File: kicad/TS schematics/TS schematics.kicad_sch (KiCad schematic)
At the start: 40 parts, among them J1 Conn_01x05, J10 Amphenol PL00Y-301-10M8, J11 Amphenol RT00104PN03, J12 Amphenol PL00X-301-10M8, J13 AT04-4P-PM11, J14 紅色儲能接綫柱100A, J15 黑色儲能接綫柱100A, J16 Amphenol PL00X-301-10M8, J17 Amphenol PL00Y-301-10M8, J19 Amphenol RT001619SNHEC03, J2 TSAL_R, J23 AT04-3P-PM05, J24 Conn_01x02, J29 Amphenol RT001619PNH, J30 Conn_01x02, J31 Conn_01x06, J33 LEM DHAB S/124, J4 TSMP, J5 Amphenol RT00122PM03, J6 Amphenol RT00122PM03, J7 Amphenol RT001619PNH, J8 DALY K40 BMS, J9 Amphenol RT0W0106PN03, K1 DISCHARGE RELAY GIGAVAC PNC11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, SW19 BOTS, U1 dumb ass dcdc 15V8A 120W, U2 CCCV 300W

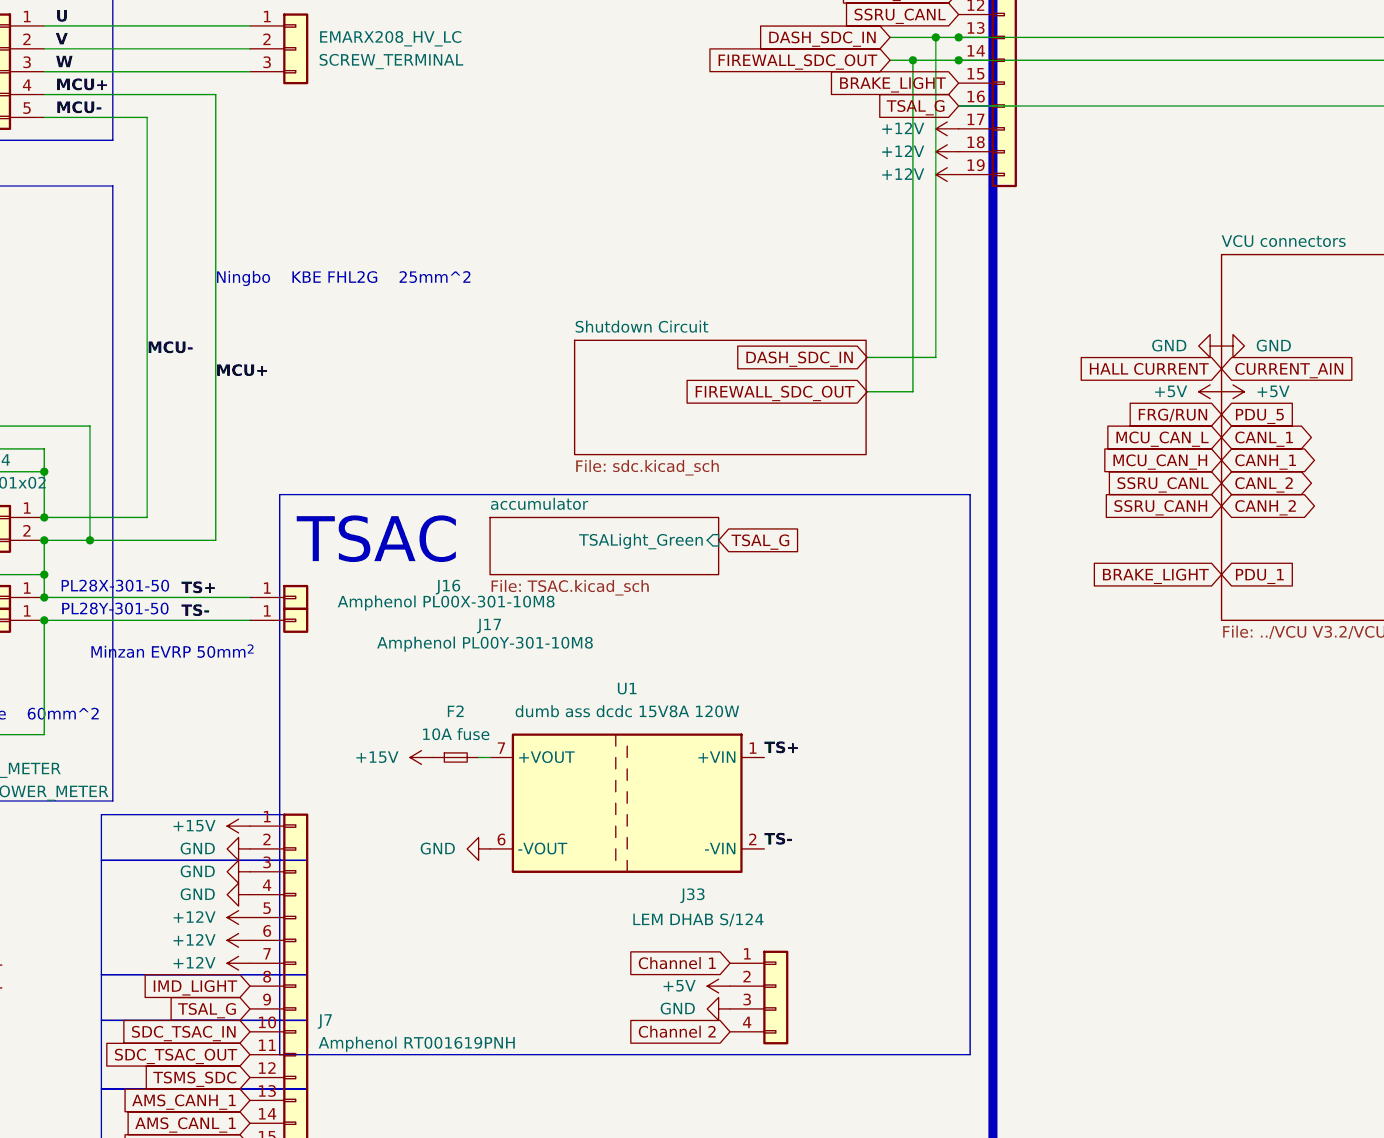
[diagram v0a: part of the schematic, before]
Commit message: what
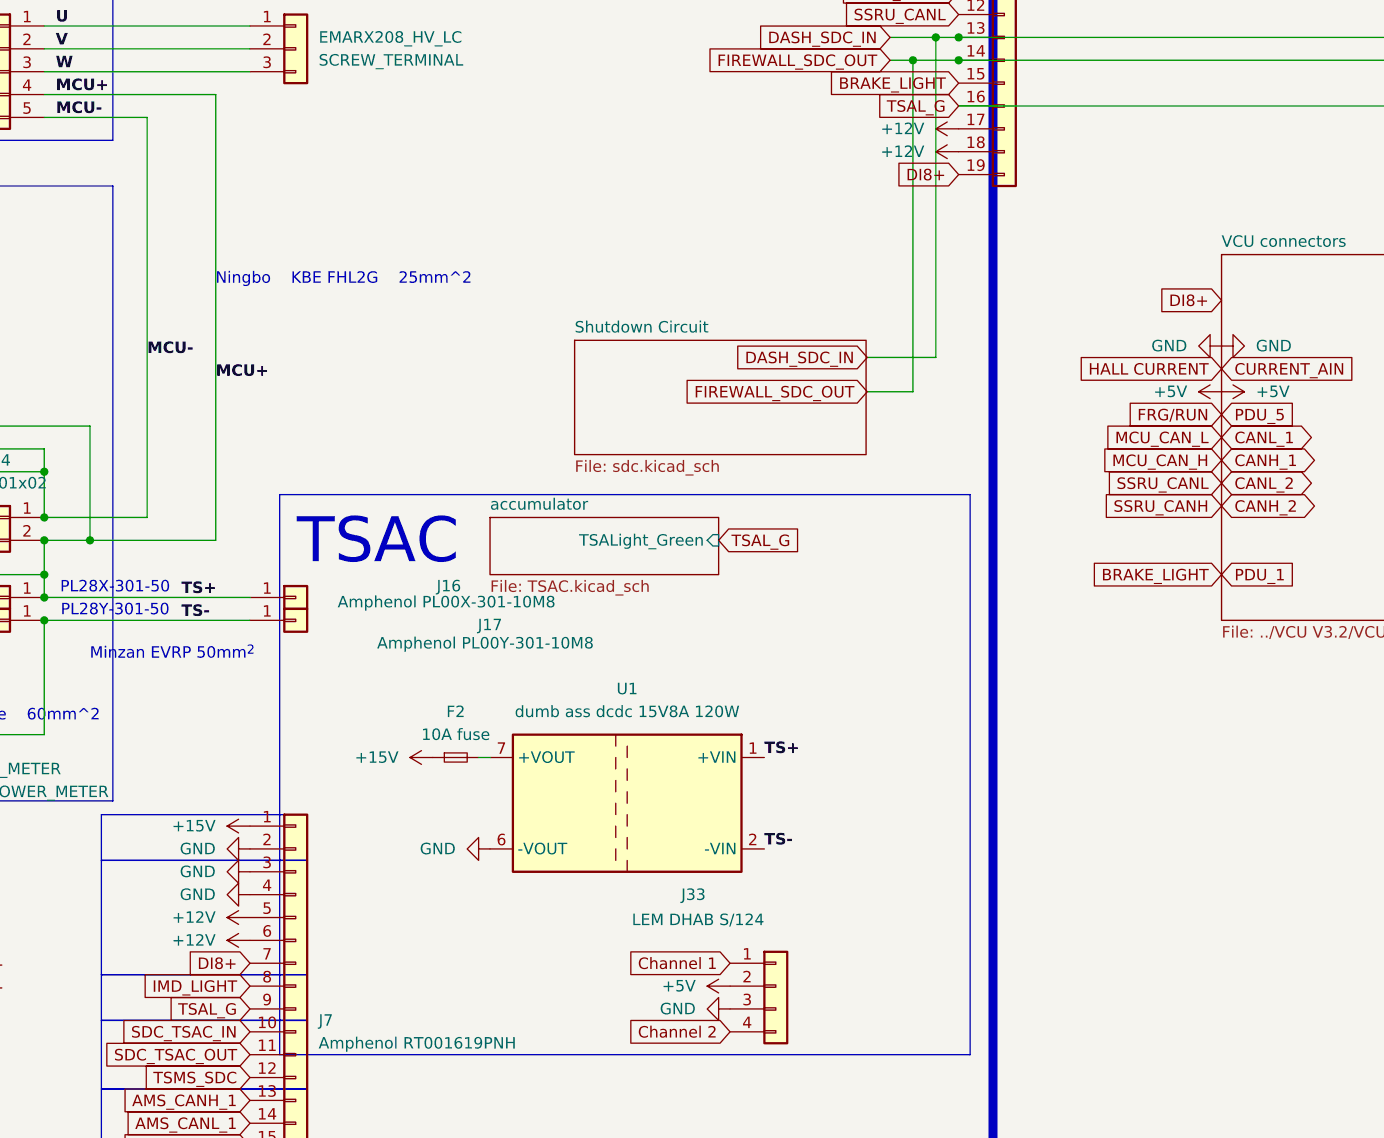
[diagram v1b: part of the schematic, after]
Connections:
- net +12V: no longer J29.19 (Pin_19), J7.7 (Pin_7)
- new net DI8+: J29.19 (Pin_19), J7.7 (Pin_7)
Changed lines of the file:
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@@
 		)
 	)
+	(global_label "DI8+"
+		(shape input)
+		(at 171.45 180.34 180)
+		(fields_autoplaced yes)
+		(effects
+			(font
+				(size 1.27 1.27)
+			)
+			(justify right)
+		)
+		(property "Intersheetrefs" "${INTERSHEET_REFS}"
+			(at 163.8081 180.34 0)
+			(effects
+				(font
+					(size 1.27 1.27)
+				)
+				(justify right)
+				(hide yes)
+			)
+		)
+	)
 	(global_label "AMS_LIGHT"
 		(shape input)
@@
 		)
 	)
+	(global_label "DI8+"
+		(shape input)
+		(at 279.4 106.68 180)
+		(fields_autoplaced yes)
+		(effects
+			(font
+				(size 1.27 1.27)
+			)
+			(justify right)
+		)
+		(property "Intersheetrefs" "${INTERSHEET_REFS}"
+			(at 271.7581 106.68 0)
+			(effects
+				(font
+					(size 1.27 1.27)
+				)
+				(justify right)
+				(hide yes)
+			)
+		)
+	)
 	(global_label "SDC_Relay"
 		(shape input)
@@
 		)
 	)
+	(global_label "DI8+"
+		(shape input)
+		(at 250.19 92.71 180)
+		(fields_autoplaced yes)
+		(effects
+			(font
+				(size 1.27 1.27)
+			)
+			(justify right)
+		)
+		(property "Intersheetrefs" "${INTERSHEET_REFS}"
+			(at 242.5481 92.71 0)
+			(effects
+				(font
+					(size 1.27 1.27)
+				)
+				(justify right)
+				(hide yes)
+			)
+		)
+	)
 	(global_label "TSAL_G"
 		(shape input)
@@
 	)
 	(symbol
-		(lib_id "power:+12V")
-		(at 250.19 92.71 90)
-		(mirror x)
-		(unit 1)
-		(exclude_from_sim no)
-		(in_bom yes)
-		(on_board yes)
-		(dnp no)
-		(fields_autoplaced yes)
-		(property "Reference" "#PWR049"
-			(at 254 92.71 0)
-			(effects
-				(font
-					(size 1.27 1.27)
-				)
-				(hide yes)
-			)
-		)
-		(property "Value" "+12V"
-			(at 246.38 92.7101 90)
-			(effects
-				(font
-					(size 1.27 1.27)
-				)
-				(justify left)
-			)
-		)
-		(property "Footprint" ""
-			(at 250.19 92.71 0)
-			(effects
-				(font
-					(size 1.27 1.27)
-				)
-				(hide yes)
-			)
-		)
-		(property "Datasheet" ""
-			(at 250.19 92.71 0)
-			(effects
-				(font
-					(size 1.27 1.27)
-				)
-				(hide yes)
-			)
-		)
-		(property "Description" "Power symbol creates a global label with name \"+12V\""
-			(at 250.19 92.71 0)
-			(effects
-				(font
-					(size 1.27 1.27)
-				)
-				(hide yes)
-			)
-		)
-		(pin "1"
-		)
-		(instances
-			(project "TS schematics"
-				(path "/55cbadab-af07-45b3-b9ce-9748abc6dcd0"
-					(reference "#PWR049")
-					(unit 1)
-				)
-			)
-		)
-	)
-	(symbol
 		(lib_id "Device:Fuse_Small")
 		(at 100.33 120.65 0)
@@
 					(unit 1)
 				)
-			)
-		)
-	)
-	(symbol
-		(lib_id "power:+12V")
-		(at 171.45 180.34 90)
-		(mirror x)
-		(unit 1)
-		(exclude_from_sim no)
-		(in_bom yes)
-		(on_board yes)
-		(dnp no)
-		(fields_autoplaced yes)
-		(property "Reference" "#PWR059"
-			(at 175.26 180.34 0)
-			(effects
-				(font
-					(size 1.27 1.27)
-				)
-				(hide yes)
-			)
-		)
-		(property "Value" "+12V"
-			(at 167.64 180.3401 90)
-			(effects
-				(font
-					(size 1.27 1.27)
-				)
-				(justify left)
-			)
-		)
-		(property "Footprint" ""
-			(at 171.45 180.34 0)
-			(effects
-				(font
-					(size 1.27 1.27)
-				)
-				(hide yes)
-			)
-		)
-		(property "Datasheet" ""
-			(at 171.45 180.34 0)
-			(effects
-				(font
-					(size 1.27 1.27)
-				)
-				(hide yes)
-			)
-		)
-		(property "Description" "Power symbol creates a global label with name \"+12V\""
-			(at 171.45 180.34 0)
-			(effects
-				(font
-					(size 1.27 1.27)
-				)
-				(hide yes)
-			)
-		)
-		(pin "1"
-		)
-		(instances
-			(project "TS schematics"
-				(path "/55cbadab-af07-45b3-b9ce-9748abc6dcd0"
-					(reference "#PWR059")
-					(unit 1)
-				)
